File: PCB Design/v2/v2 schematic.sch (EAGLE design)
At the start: 9 parts

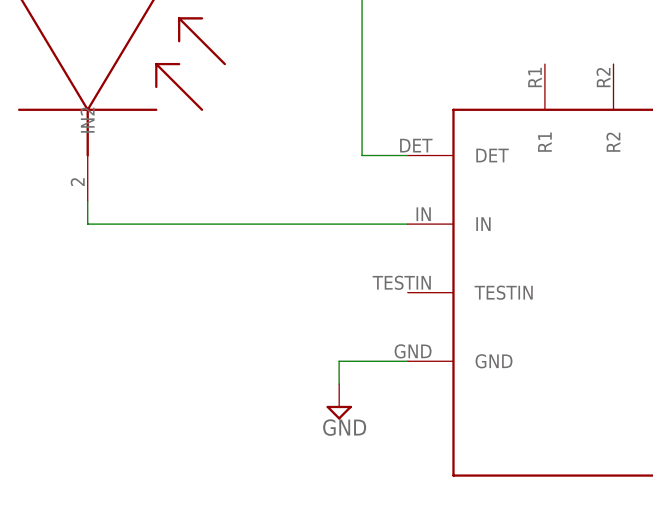
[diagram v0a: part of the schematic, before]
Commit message: Added SHARD-1 Library
Finalised v2 board for manufacturing.

Signed-off-by: joncrabb <jc00300@surrey.ac.uk>
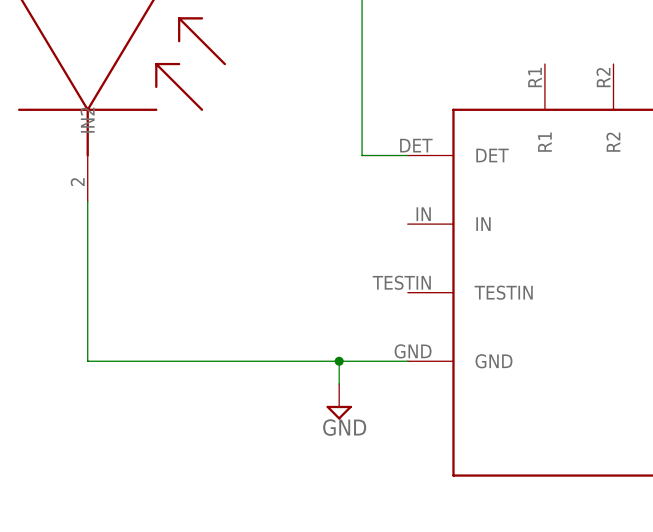
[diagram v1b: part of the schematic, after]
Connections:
- removed net N$5: PC21.IN, PINDIODE.IN2
- net GND: now also PINDIODE.IN2
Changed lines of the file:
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@@
 </classes>
 <parts>
-<part name="PC21" library="SHARD" deviceset="A111" device=""/>
 <part name="45V" library="keystone" deviceset="TP" device="-063"/>
 <part name="30V1" library="keystone" deviceset="TP" device="-063"/>
@@
 <part name="SUPPLY3" library="supply2" deviceset="GND" device=""/>
 <part name="PINDIODE" library="SHARD" deviceset="S3590-08" device=""/>
+<part name="PC21" library="SHARD" deviceset="A111" device=""/>
 </parts>
 <sheets>
@@
 </plain>
 <instances>
-<instance part="PC21" gate="G$1" x="0" y="0"/>
 <instance part="45V" gate="G$1" x="7.62" y="38.1"/>
 <instance part="30V1" gate="G$1" x="7.62" y="45.72" rot="R180"/>
@@
 <instance part="SUPPLY3" gate="GND" x="60.96" y="-20.32"/>
 <instance part="PINDIODE" gate="G$1" x="-60.96" y="20.32" rot="R270"/>
+<instance part="PC21" gate="G$1" x="0" y="0"/>
 </instances>
 <busses>
@@
 <net name="N$1" class="0">
 <segment>
-<pinref part="PC21" gate="G$1" pin="HV"/>
 <wire x1="7.62" y1="25.4" x2="7.62" y2="35.56" width="0.1524" layer="91"/>
 <pinref part="45V" gate="G$1" pin="1"/>
+<pinref part="PC21" gate="G$1" pin="HV"/>
 </segment>
 </net>
@@
 </segment>
 <segment>
-<pinref part="PC21" gate="G$1" pin="GND"/>
 <pinref part="SUPPLY2" gate="GND" pin="GND"/>
 <wire x1="-25.4" y1="-7.62" x2="-33.02" y2="-7.62" width="0.1524" layer="91"/>
 <wire x1="-33.02" y1="-7.62" x2="-33.02" y2="-10.16" width="0.1524" layer="91"/>
+<pinref part="PC21" gate="G$1" pin="GND"/>
+<pinref part="PINDIODE" gate="G$1" pin="IN2"/>
+<wire x1="-60.96" y1="10.16" x2="-60.96" y2="-7.62" width="0.1524" layer="91"/>
+<wire x1="-60.96" y1="-7.62" x2="-33.02" y2="-7.62" width="0.1524" layer="91"/>
+<junction x="-33.02" y="-7.62"/>
 </segment>
 <segment>
-<pinref part="PC21" gate="G$1" pin="GNDOUT1"/>
 <pinref part="SUPPLY3" gate="GND" pin="GND"/>
 <wire x1="25.4" y1="-5.08" x2="60.96" y2="-5.08" width="0.1524" layer="91"/>
@@
 <wire x1="55.88" y1="-15.24" x2="60.96" y2="-15.24" width="0.1524" layer="91"/>
 <junction x="60.96" y="-15.24"/>
-<pinref part="PC21" gate="G$1" pin="GNDOUT0"/>
 <wire x1="25.4" y1="10.16" x2="60.96" y2="10.16" width="0.1524" layer="91"/>
 <wire x1="60.96" y1="10.16" x2="60.96" y2="-5.08" width="0.1524" layer="91"/>
 <junction x="60.96" y="-5.08"/>
+<pinref part="PC21" gate="G$1" pin="GNDOUT1"/>
+<pinref part="PC21" gate="G$1" pin="GNDOUT0"/>
 </segment>
 </net>
 <net name="N$4" class="0">
 <segment>
-<pinref part="PC21" gate="G$1" pin="VS"/>
 <pinref part="G1" gate="G$1" pin="+"/>
 <wire x1="25.4" y1="-10.16" x2="25.4" y2="-15.24" width="0.1524" layer="91"/>
 <wire x1="25.4" y1="-15.24" x2="30.48" y2="-15.24" width="0.1524" layer="91"/>
-</segment>
-</net>
-<net name="N$5" class="0">
-<segment>
-<pinref part="PINDIODE" gate="G$1" pin="IN2"/>
-<pinref part="PC21" gate="G$1" pin="IN"/>
-<wire x1="-60.96" y1="10.16" x2="-60.96" y2="7.62" width="0.1524" layer="91"/>
-<wire x1="-60.96" y1="7.62" x2="-25.4" y2="7.62" width="0.1524" layer="91"/>
+<pinref part="PC21" gate="G$1" pin="VS"/>
 </segment>
 </net>
@@
 <pinref part="PINDIODE" gate="G$1" pin="IN1"/>
 <wire x1="-60.96" y1="48.26" x2="-30.48" y2="48.26" width="0.1524" layer="91"/>
-<pinref part="PC21" gate="G$1" pin="DET"/>
 <wire x1="-30.48" y1="48.26" x2="-30.48" y2="15.24" width="0.1524" layer="91"/>
 <wire x1="-30.48" y1="15.24" x2="-25.4" y2="15.24" width="0.1524" layer="91"/>
+<pinref part="PC21" gate="G$1" pin="DET"/>
 </segment>
 </net>

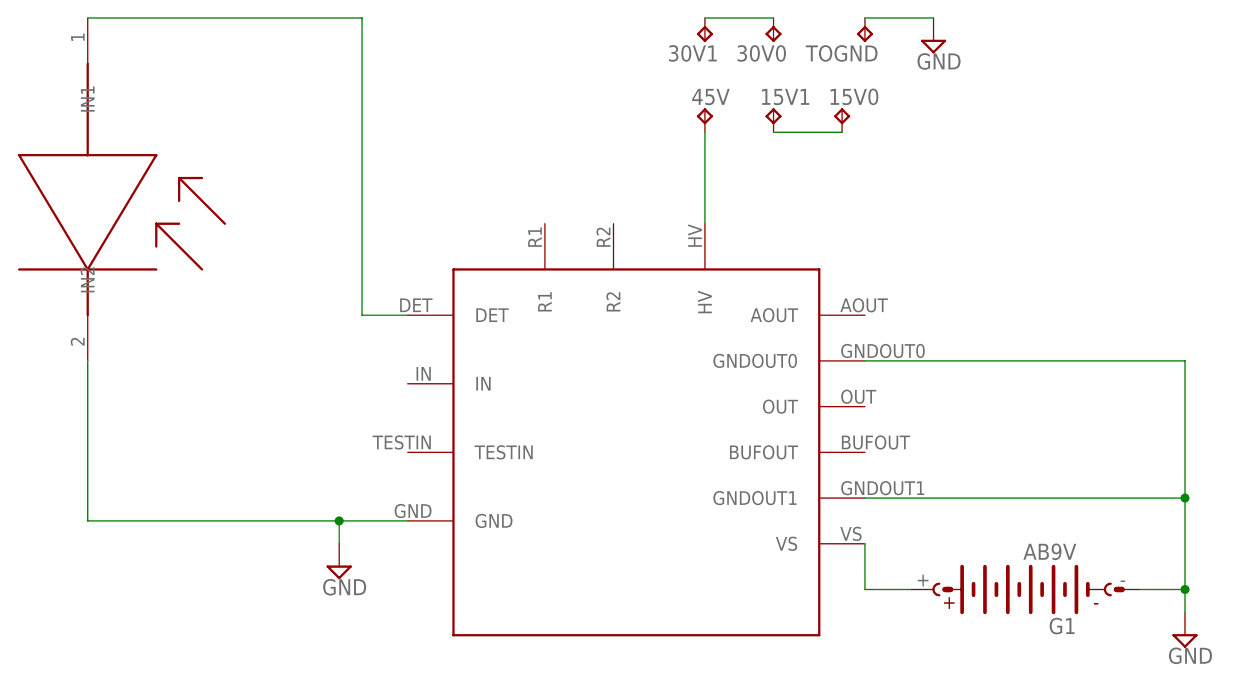
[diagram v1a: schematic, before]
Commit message: Updated PCB design so diode is now reversed bias (correct)
Signed-off-by: joncrabb <jc00300@surrey.ac.uk>
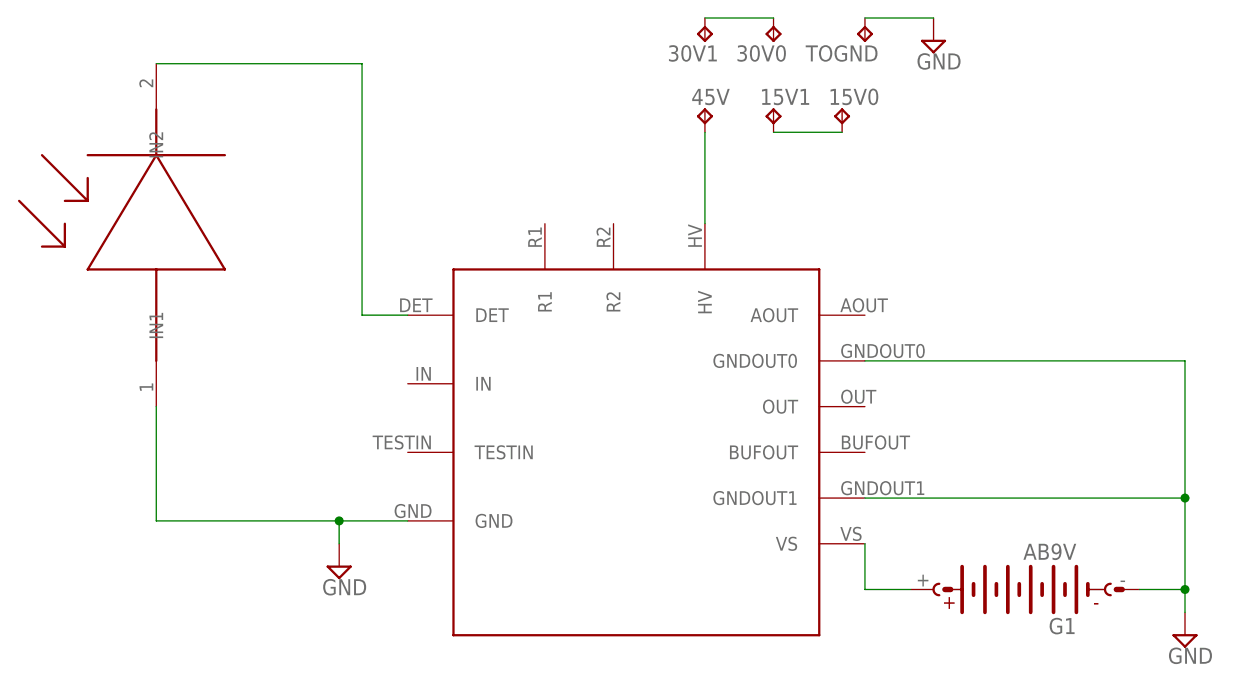
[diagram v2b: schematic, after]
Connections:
- net GND: now also PINDIODE.IN1; no longer PINDIODE.IN2
- net N$6: now also PINDIODE.IN2; no longer PINDIODE.IN1
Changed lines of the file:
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@@
 <instance part="G1" gate="G$1" x="43.18" y="-15.24" rot="R180"/>
 <instance part="SUPPLY3" gate="GND" x="60.96" y="-20.32"/>
-<instance part="PINDIODE" gate="G$1" x="-60.96" y="20.32" rot="R270"/>
+<instance part="PINDIODE" gate="G$1" x="-53.34" y="33.02" rot="R90"/>
 <instance part="PC21" gate="G$1" x="0" y="0"/>
 </instances>
@@
 <segment>
 <pinref part="SUPPLY2" gate="GND" pin="GND"/>
+<wire x1="-33.02" y1="-7.62" x2="-33.02" y2="-10.16" width="0.1524" layer="91"/>
 <wire x1="-25.4" y1="-7.62" x2="-33.02" y2="-7.62" width="0.1524" layer="91"/>
-<wire x1="-33.02" y1="-7.62" x2="-33.02" y2="-10.16" width="0.1524" layer="91"/>
 <pinref part="PC21" gate="G$1" pin="GND"/>
-<pinref part="PINDIODE" gate="G$1" pin="IN2"/>
-<wire x1="-60.96" y1="10.16" x2="-60.96" y2="-7.62" width="0.1524" layer="91"/>
-<wire x1="-60.96" y1="-7.62" x2="-33.02" y2="-7.62" width="0.1524" layer="91"/>
+<pinref part="PINDIODE" gate="G$1" pin="IN1"/>
+<wire x1="-33.02" y1="-7.62" x2="-53.34" y2="-7.62" width="0.1524" layer="91"/>
+<wire x1="-53.34" y1="-7.62" x2="-53.34" y2="5.08" width="0.1524" layer="91"/>
 <junction x="-33.02" y="-7.62"/>
 </segment>
@@
 <net name="N$6" class="0">
 <segment>
-<pinref part="PINDIODE" gate="G$1" pin="IN1"/>
-<wire x1="-60.96" y1="48.26" x2="-30.48" y2="48.26" width="0.1524" layer="91"/>
-<wire x1="-30.48" y1="48.26" x2="-30.48" y2="15.24" width="0.1524" layer="91"/>
+<wire x1="-30.48" y1="43.18" x2="-30.48" y2="15.24" width="0.1524" layer="91"/>
 <wire x1="-30.48" y1="15.24" x2="-25.4" y2="15.24" width="0.1524" layer="91"/>
 <pinref part="PC21" gate="G$1" pin="DET"/>
+<pinref part="PINDIODE" gate="G$1" pin="IN2"/>
+<wire x1="-53.34" y1="43.18" x2="-30.48" y2="43.18" width="0.1524" layer="91"/>
 </segment>
 </net>
